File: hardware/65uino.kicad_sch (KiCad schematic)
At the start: 54 parts, among them J1 Barrel_Jack_MountingPin, J2 USB_B_Micro, J3 OLED, SW1 RST, SW2 BTN, U1 R6507, U2 NC/74HC04, U3 6532, U4 w27C512, U5 MIC5504-3.3YM5, U6 LM1117-5.0, U7 SN74LVC1G14DBVR, X1 1MHz, Y1 NC/1Mhz

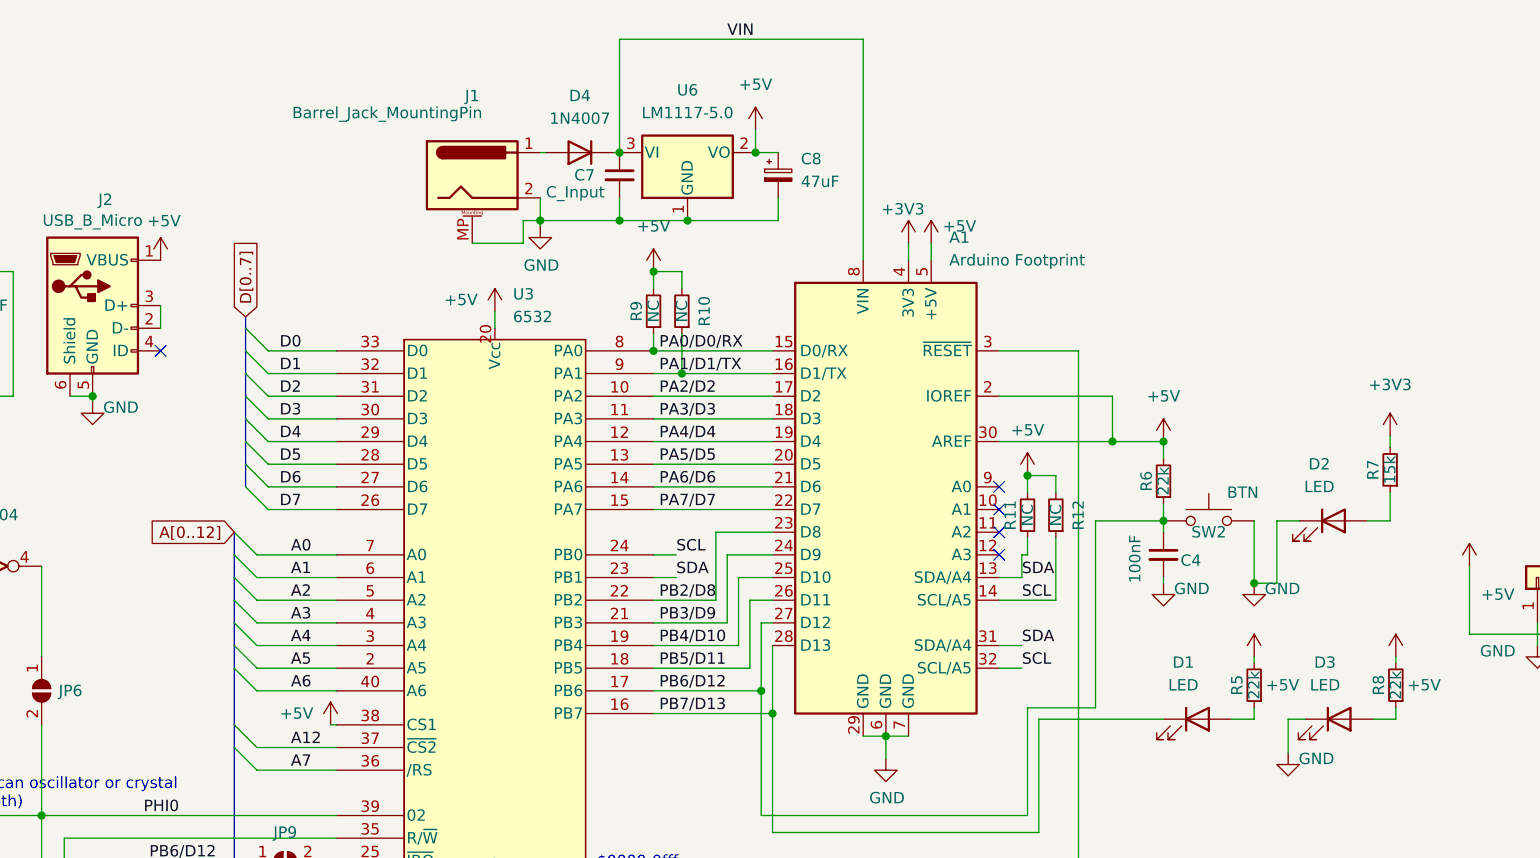
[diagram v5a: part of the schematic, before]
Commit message: Manufacturing improvements
MicroUSB changed to Amphenol 10118194
5V regulator capacitors changed to 1206 10uF
LCSC Parts numbers added
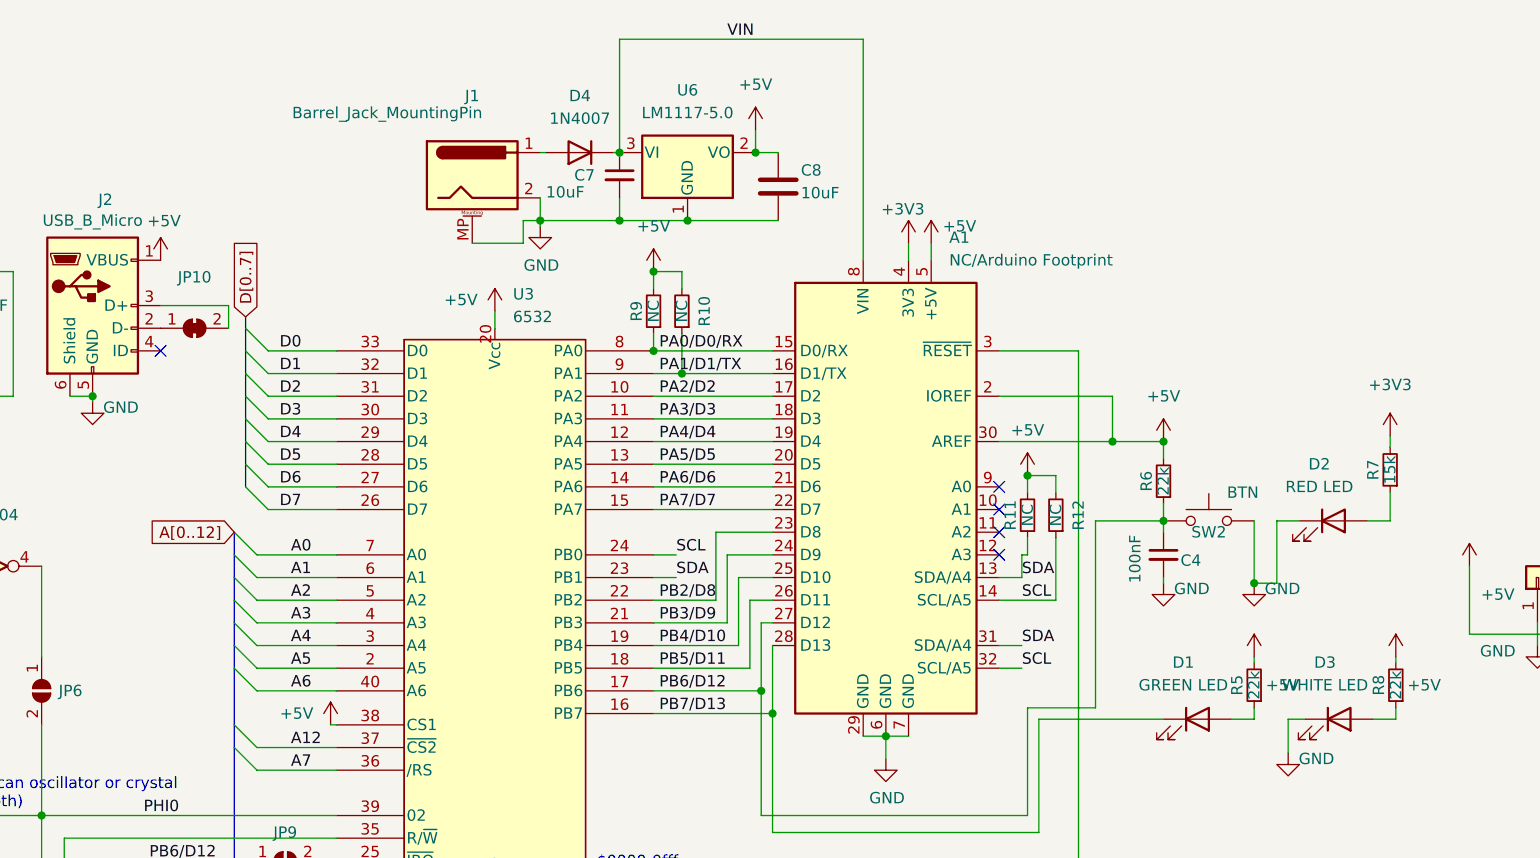
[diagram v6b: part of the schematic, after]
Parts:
- added JP10: SolderJumper_2_Bridged, Jumper:SolderJumper-2_P1.3mm_Bridged_RoundedPad1.0x1.5mm, symbol Jumper:SolderJumper_2_Bridged
- A1: value Arduino Footprint -> NC/Arduino Footprint
- C11, C12, C13, C3, C4, C9: LCSC (none) -> C49678
- C5, C6: LCSC (none) -> C28323
- C7: value C_Input -> 10uF; footprint Capacitor_SMD:C_0805_2012Metric -> Capacitor_SMD:C_1206_3216Metric; LCSC (none) -> C13585
- C8: value 47uF -> 10uF; footprint Capacitor_SMD:CP_Elec_6.3x7.7 -> Capacitor_SMD:C_1206_3216Metric; symbol Device:C_Polarized_Small -> Device:C; LCSC (none) -> C13585
- D1: value LED -> GREEN LED; LCSC (none) -> C2297
- D2: value LED -> RED LED; LCSC (none) -> C84256
- D3: value LED -> WHITE LED; LCSC (none) -> C34499
- D4: footprint Diode_SMD:D_SMB -> Diode_SMD:D_SMA; LCSC (none) -> C95872
- J2: footprint Connector_USB:USB-B-MICRO-SMD_V03-fixed -> Connector_USB:USB_Micro-B_Amphenol_10118194_Horizontal; LCSC (none) -> C132563
- R1, R2: LCSC (none) -> C17661
- R5, R6, R8: LCSC (none) -> C17560
- R7: LCSC (none) -> C17475
- SW1, SW2: LCSC (none) -> C318884
- U5: LCSC (none) -> C3021093
- U6: LCSC (none) -> C6187
- U7: LCSC (none) -> C434069
- X1: LCSC (none) -> C390529
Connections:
- net at J2.2 (D-): now also JP10.1 (A); no longer J2.3 (D+)
- new net: J2.3 (D+), JP10.2 (B)

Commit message: Minor
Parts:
- U6: value LM1117-5.0 -> AMS1117-5.0; LCSC C6187 -> C347223
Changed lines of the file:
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@@
     (in_bom yes) (on_board yes) (fields_autoplaced)
     (property "Reference" "U6" (id 0) (at 160.02 24.13 0))
-    (property "Value" "LM1117-5.0" (id 1) (at 160.02 26.67 0))
+    (property "Value" "AMS1117-5.0" (id 1) (at 160.02 26.67 0))
     (property "Footprint" "Package_TO_SOT_SMD:SOT-223-3_TabPin2" (id 2) (at 160.02 31.115 0)
       (effects (font (size 1.27 1.27)) hide)
@@
       (effects (font (size 1.27 1.27)) hide)
     )
-    (property "LCSC" "C6187" (id 4) (at 160.02 31.115 0)
+    (property "LCSC" "C347223" (id 4) (at 160.02 31.115 0)
       (effects (font (size 1.27 1.27)) hide)
     )
@@
     )
     (path "/9bf119ff-e802-4129-8881-127b8b78b865"
-      (reference "U6") (unit 1) (value "LM1117-5.0") (footprint "Package_TO_SOT_SMD:SOT-223-3_TabPin2")
+      (reference "U6") (unit 1) (value "AMS1117-5.0") (footprint "Package_TO_SOT_SMD:SOT-223-3_TabPin2")
     )
     (path "/ce8dc6a6-9429-47a9-9065-d7f01396ec1a"

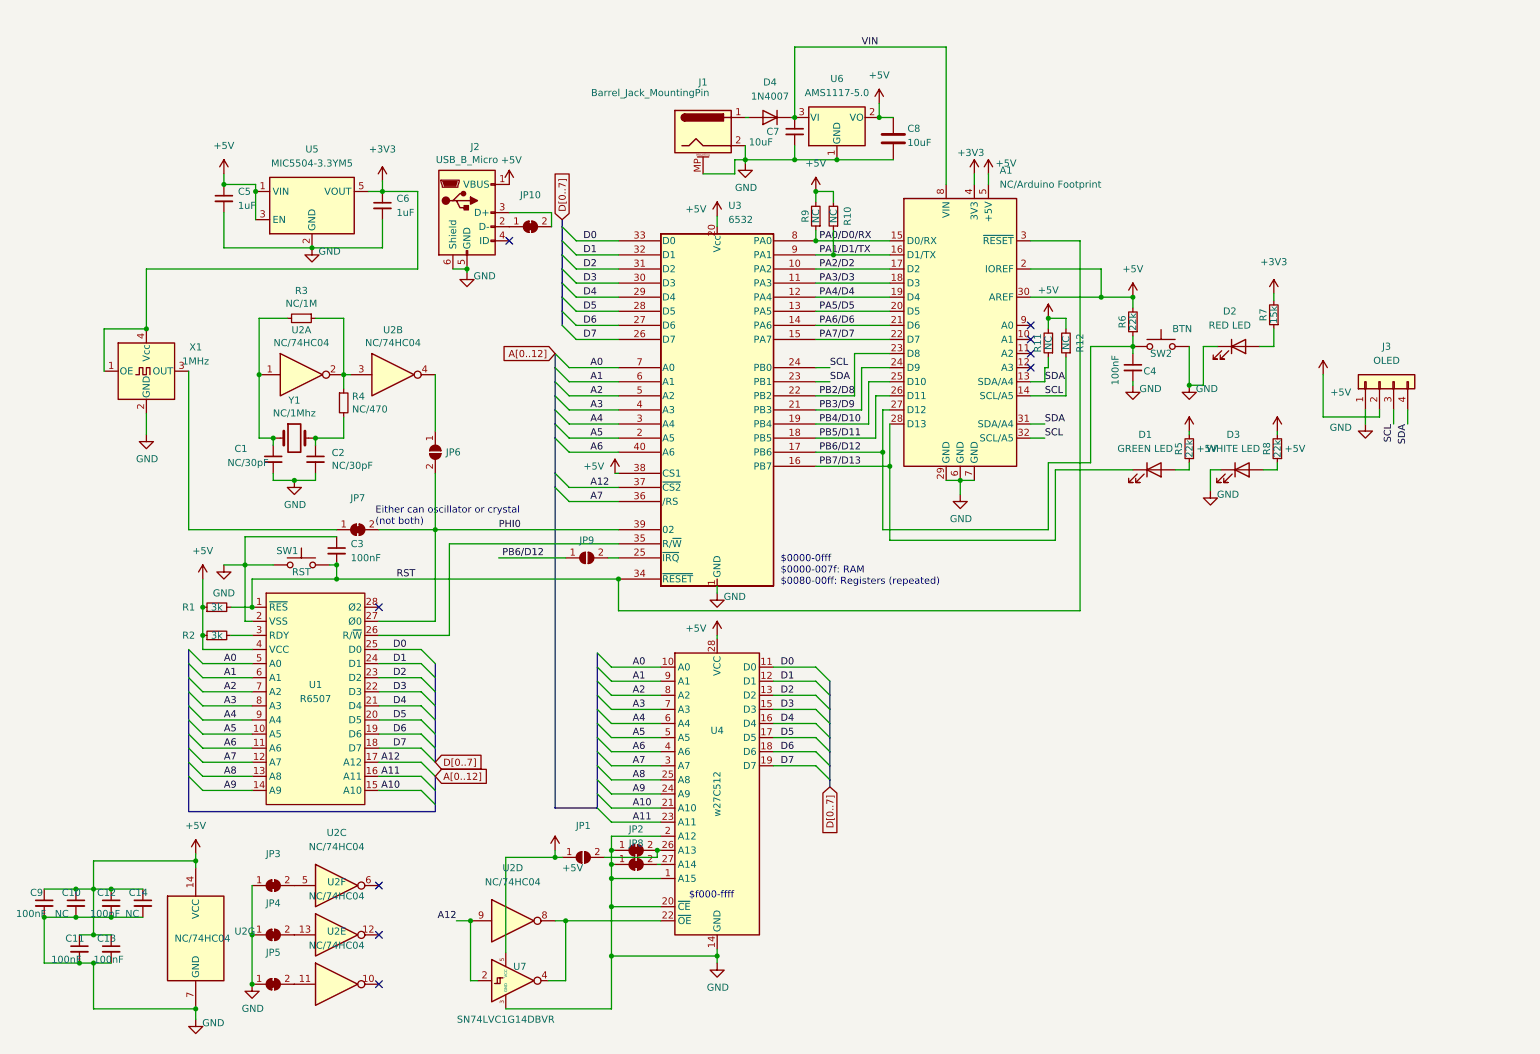
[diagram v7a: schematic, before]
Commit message: Revision 1 - UART & Clock Divider
UART, Clock Divider, extra address decoding and bus headers added - a full-fledged 6502 computer with an Uno footprint!
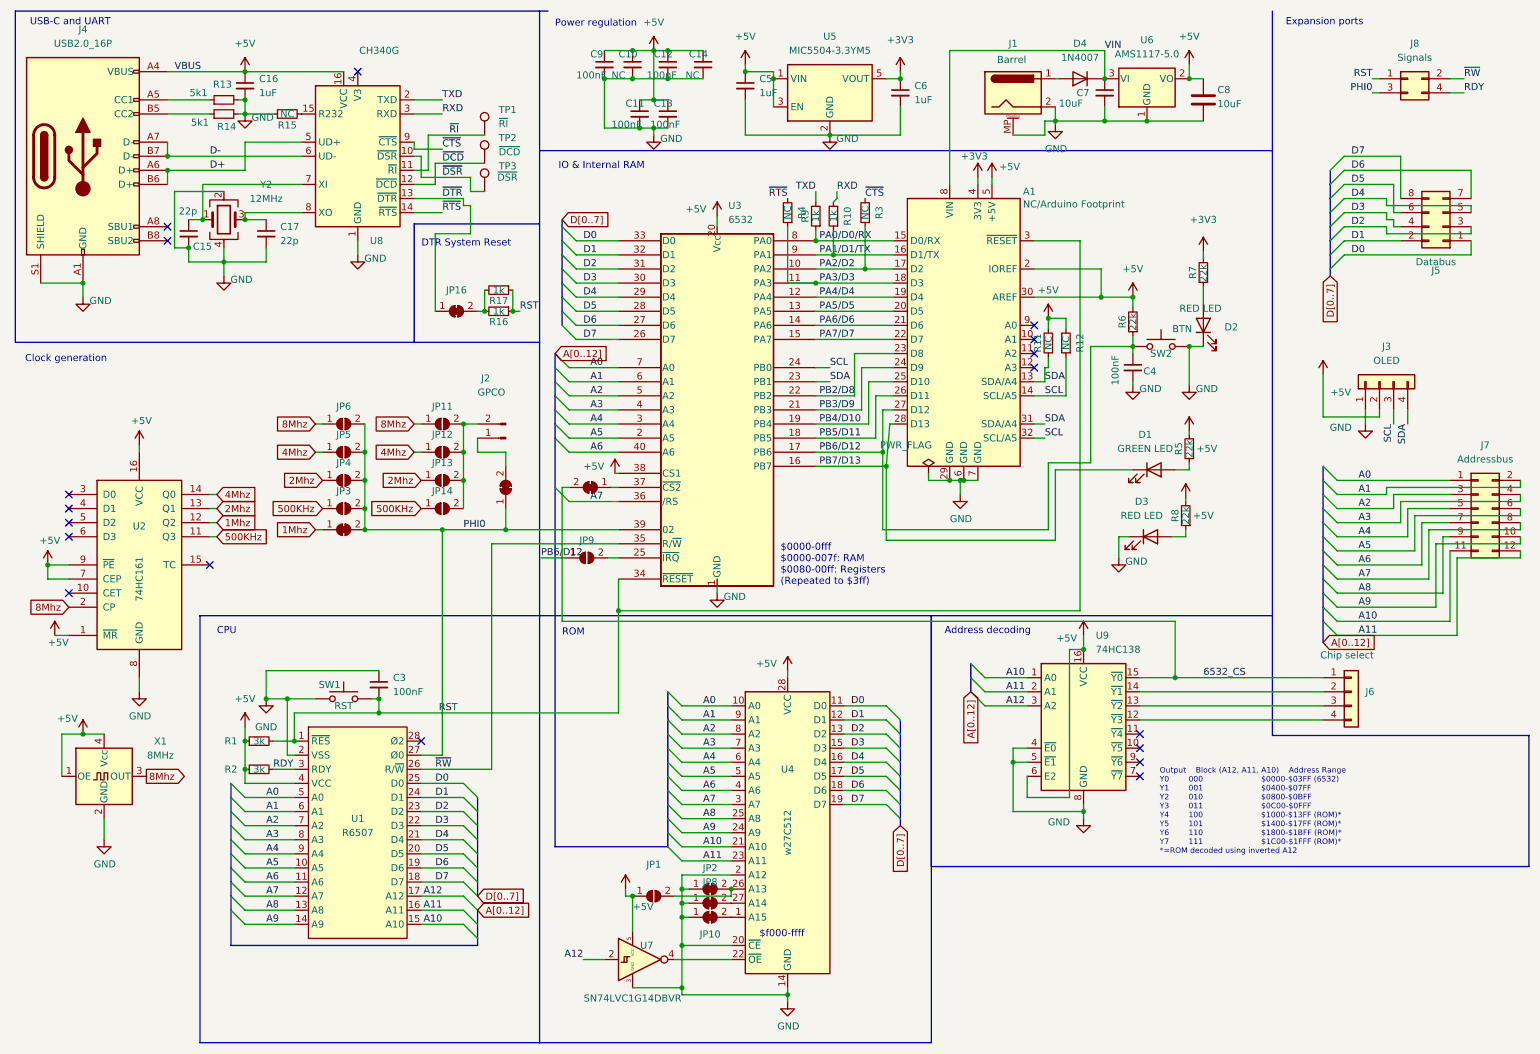
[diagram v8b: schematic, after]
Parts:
- removed C1, C2: NC/30pF, Capacitor_SMD:C_0805_2012Metric, symbol Device:C_Small
- removed J2: USB_B_Micro, Connector_USB:USB_Micro-B_Amphenol_10118194_Horizontal, symbol 6502-rescue:USB_B_Micro-Connector
- removed JP3, JP4, JP5: SolderJumper_2_Bridged, Jumper:SolderJumper-2_P1.3mm_Bridged_RoundedPad1.0x1.5mm, symbol Jumper:SolderJumper_2_Bridged
- removed U2: NC/74HC04, Package_DIP:DIP-14_W7.62mm, symbol 74xx:74HC04
- removed Y1: NC/1Mhz, Crystal:Crystal_HC49-U_Vertical, symbol Device:Crystal
- added C15, C17: 22p, Capacitor_SMD:C_0805_2012Metric, symbol Device:C_Small
- added C16: 1uF, Capacitor_SMD:C_0805_2012Metric, symbol Device:C_Small
- added J2: GPCO, Connector_PinHeader_2.54mm:PinHeader_1x02_P2.54mm_Vertical, symbol Connector:Conn_01x02_Pin
- added J4: USB2.0_16P, Connector_USB:USB_C_Receptacle_HCTL_HC-TYPE-C-16P-01A, symbol Connector:USB_C_Receptacle_USB2.0_16P
- added J5: Databus, Connector_PinHeader_2.54mm:PinHeader_2x04_P2.54mm_Vertical, symbol Connector_Generic:Conn_02x04_Odd_Even
- added J6: Chip select, Connector_PinSocket_2.54mm:PinSocket_1x04_P2.54mm_Vertical, symbol Connector_Generic:Conn_01x04
- added J7: Addressbus, Connector_PinHeader_2.54mm:PinHeader_2x06_P2.54mm_Vertical, symbol Connector_Generic:Conn_02x06_Odd_Even
- added J8: Signals, Connector_PinHeader_2.54mm:PinHeader_2x02_P2.54mm_Vertical, symbol Connector_Generic:Conn_02x02_Odd_Even
- added JP11, JP12, JP13, JP14, JP3, JP4, JP5: SolderJumper_2_Bridged, Jumper:SolderJumper-2_P1.3mm_Open_RoundedPad1.0x1.5mm, symbol Jumper:SolderJumper_2_Open
- added JP15, JP16, JP17: SolderJumper_2_Bridged, Jumper:SolderJumper-2_P1.3mm_Bridged_RoundedPad1.0x1.5mm, symbol Jumper:SolderJumper_2_Bridged
- added R13, R14: 5k1, Resistor_SMD:R_0805_2012Metric, symbol Device:R_Small
- added R15: NC, Resistor_SMD:R_0805_2012Metric, symbol Device:R_Small
- added R16, R17: 1k, Resistor_SMD:R_0805_2012Metric, symbol Device:R_Small
- added TP1: ~{RI}, TestPoint:TestPoint_Pad_D1.0mm, symbol Connector:TestPoint
- added TP2: ~{DCD}, TestPoint:TestPoint_Pad_D1.0mm, symbol Connector:TestPoint
- added TP3: ~{DSR}, TestPoint:TestPoint_Pad_D1.0mm, symbol Connector:TestPoint
- added U2: 74HC161, Package_SO:SOP-16_3.9x9.9mm_P1.27mm, symbol 74xx:74LS161
- added U8: CH340G, Package_SO:SOIC-16_3.9x9.9mm_P1.27mm, symbol Interface_USB:CH340G
- added U9: 74HC138, Package_SO:SOP-16_3.9x9.9mm_P1.27mm, symbol 74xx:74HC138
- added Y2: 12MHz, Crystal:Crystal_SMD_3225-4Pin_3.2x2.5mm, symbol Device:Crystal_GND24
- D3: value WHITE LED -> RED LED; LCSC C34499 -> C84256
- J1: value Barrel_Jack_MountingPin -> Barrel
- R10, R9: value NC -> 1k
- R3: value NC/1M -> NC
- R4: value NC/470 -> NC
- R7: value 15k -> 22k
- U1, U4: LCSC (none) -> C72121
- U3: LCSC (none) -> C72123
- X1: value 1MHz -> 8MHz; footprint Oscillator:Oscillator_SMD_SeikoEpson_SG210-4Pin_2.5x2.0mm_HandSoldering -> Crystal:Crystal_SMD_3225-4Pin_3.2x2.5mm; LCSC C390529 -> C454610
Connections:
- net +3V3: no longer X1.1 (OE), X1.4 (Vcc)
- net +5V: now also X1.1 (OE), X1.4 (Vcc), C16.1, J4.A4 (VBUS), J4.A9 (VBUS), J4.B4 (VBUS), J4.B9 (VBUS), U2.1 (~{MR}), U2.16 (VCC), U2.7 (CEP), U2.9 (~{PE}), U8.16 (VCC), U9.16 (VCC), U9.6 (E2); no longer R10.2, R9.2
- net A0: now also J7.1 (Pin_1)
- net A1: now also J7.2 (Pin_2)
- net A10: now also J7.11 (Pin_11), U9.1 (A0)
- net A11: now also J7.12 (Pin_12), U9.2 (A1)
- net A12: now also U9.3 (A2); no longer U3.37 (~{CS2})
- net A2: now also J7.3 (Pin_3)
- net A3: now also J7.4 (Pin_4)
- net A4: now also J7.5 (Pin_5)
- net A5: now also J7.6 (Pin_6)
- net A6: now also J7.7 (Pin_7)
- net A7: now also J7.8 (Pin_8)
- net A8: now also J7.9 (Pin_9)
- net A9: now also J7.10 (Pin_10)
- net D0: now also J5.1 (Pin_1)
- net D1: now also J5.2 (Pin_2)
- net D2: now also J5.3 (Pin_3)
- net D3: now also J5.4 (Pin_4)
- net D4: now also J5.5 (Pin_5)
- net D5: now also J5.6 (Pin_6)
- net D6: now also J5.7 (Pin_7)
- net D7: now also J5.8 (Pin_8)
- net GND: now also JP10.1 (A), C15.2, C16.2, C17.2, J4.A1 (GND), J4.A12 (GND), J4.B1 (GND), J4.B12 (GND), J4.S1 (SHIELD), R13.2, R14.2, R15.1, U2.8 (GND), U8.1 (GND), U9.4 (~{E0}), U9.5 (~{E1}), U9.8 (GND), Y2.2, Y2.4; no longer U4.1 (A15)
- net PA2/D2: now also R3.1
- net PA3/D3: now also R4.1
- net PHI0: now also J8.3 (Pin_3), JP15.1 (A), JP3.2 (B), JP4.2 (B), JP5.2 (B)
- net RST: now also J8.1 (Pin_1), R16.1, R17.1
- net 1Mhz: now reaches JP7.1 (A)
- net 1Mhz: now also U2.12 (Q2); no longer X1.3 (OUT)
- net 8Mhz: now reaches JP6.1 (A)
- net 8Mhz: now also X1.3 (OUT), JP11.1 (A), U2.2 (CP)
- net RDY: now reaches R2.2, U1.3 (RDY)
- net RDY: now also J8.4 (Pin_4)
- net ~{CTS}: now reaches R3.2
- net ~{CTS}: now also U8.9 (~{CTS})
- net at JP10.2 (B): now also U4.1 (A15)
- net ~{RTS}: now reaches R4.2
- net ~{RTS}: now also U8.14 (~{RTS})
- net ~{RW}: now reaches U1.26 (R/~{W}), U3.35 (R/~{W})
- net ~{RW}: now also J8.2 (Pin_2)
- new net: JP16.2 (B), R16.2, R17.2
- new net: J4.B5 (CC2), R14.1
- new net: J2.1 (Pin_1), JP15.2 (B)
- new net: R15.2, U8.15 (R232)
- new net: C15.1, U8.7 (XI), Y2.1
- new net: C17.1, U8.8 (XO), Y2.3
- new net: J2.2 (Pin_2), JP11.2 (B), JP12.2 (B), JP13.2 (B), JP14.2 (B)
- new net: JP17.1 (A), U3.37 (~{CS2})
- new net: J6.2 (Pin_2), U9.14 (~{Y1})
- new net: J6.3 (Pin_3), U9.13 (~{Y2})
- new net: J6.4 (Pin_4), U9.12 (~{Y3})
- new net: J4.A5 (CC1), R13.1
- new net 2Mhz: JP13.1 (A), JP4.1 (A), U2.13 (Q1)
- new net 4Mhz: JP12.1 (A), JP5.1 (A), U2.14 (Q0)
- new net 500KHz: JP14.1 (A), JP3.1 (A), U2.11 (Q3)
- new net 6532_CS: J6.1 (Pin_1), JP17.2 (B), U9.15 (~{Y0})
- new net D+: J4.A6 (D+), J4.B6 (D+), U8.5 (UD+)
- new net D-: J4.A7 (D-), J4.B7 (D-), U8.6 (UD-)
- new net RXD: R10.2, U8.3 (RXD)
- new net TXD: R9.2, U8.2 (TXD)
- new net ~{DCD}: TP2.1, U8.12 (~{DCD})
- new net ~{DSR}: TP3.1, U8.10 (~{DSR})
- new net ~{DTR}: JP16.1 (A), U8.13 (~{DTR})
- new net ~{RI}: TP1.1, U8.11 (~{RI})
- no-connect marks 9 -> 18
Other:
- note added: "$0000-0fff $0000-007f: RAM $0080-00ff: Registers (Repeated to $3ff)"
- note added: "Address decoding"
- note added: "CPU"
- note added: "Clock generation"
- note added: "DTR System Reset"
- note added: "Expansion ports"
- note added: "IO & Internal RAM"
- note added: "Output Block (A12, A11, A10) Address Range Y0 000 $0000-$03FF (6532) Y1 001 $0400-$07FF Y2 010 $0800-$0BFF Y3 011 $0C00-$0FFF Y4 100 $1000-$13FF (ROM)* Y5 101 $1400-$17FF (ROM)* Y6 110 $1800-$1BFF (ROM)* Y7 111 $1C00-$1FFF (ROM)* *=ROM decoded using inverted A12"
- note added: "Power regulation"
- note added: "ROM"
- note added: "USB-C and UART"
- note removed: "$0000-0fff $0000-007f: RAM $0080-00ff: Registers (repeated)"
- note removed: "Either can oscillator or crystal (not both)"
- moved on the sheet: A1, C10, C11, C12, C13, C14, C3, C5, C6, C7, C8, C9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
